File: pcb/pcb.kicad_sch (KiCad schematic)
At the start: 41 parts, among them J1 NMJ4HCD2, J2 NMJ4HCD2, J3 694106301002, SW1 FSWITCH, U1 RC4558, U2 L78L09_TO92

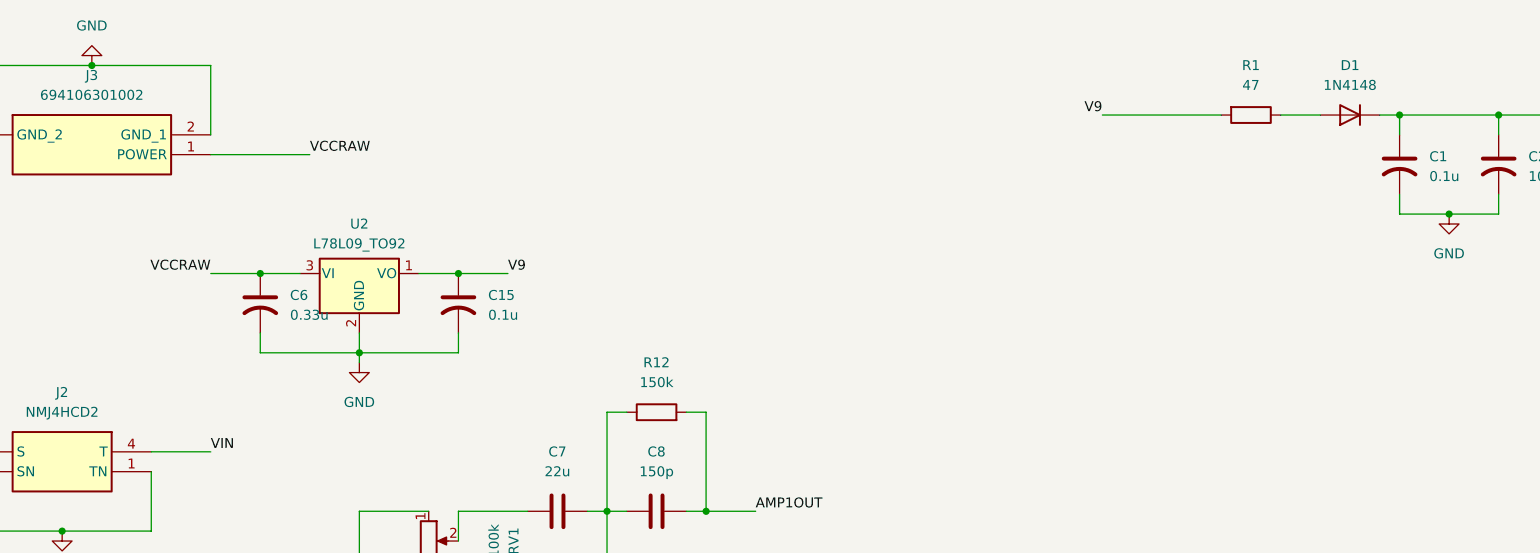
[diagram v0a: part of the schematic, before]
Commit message: Fix reverse polarity protection diode - Move ahead of regulator
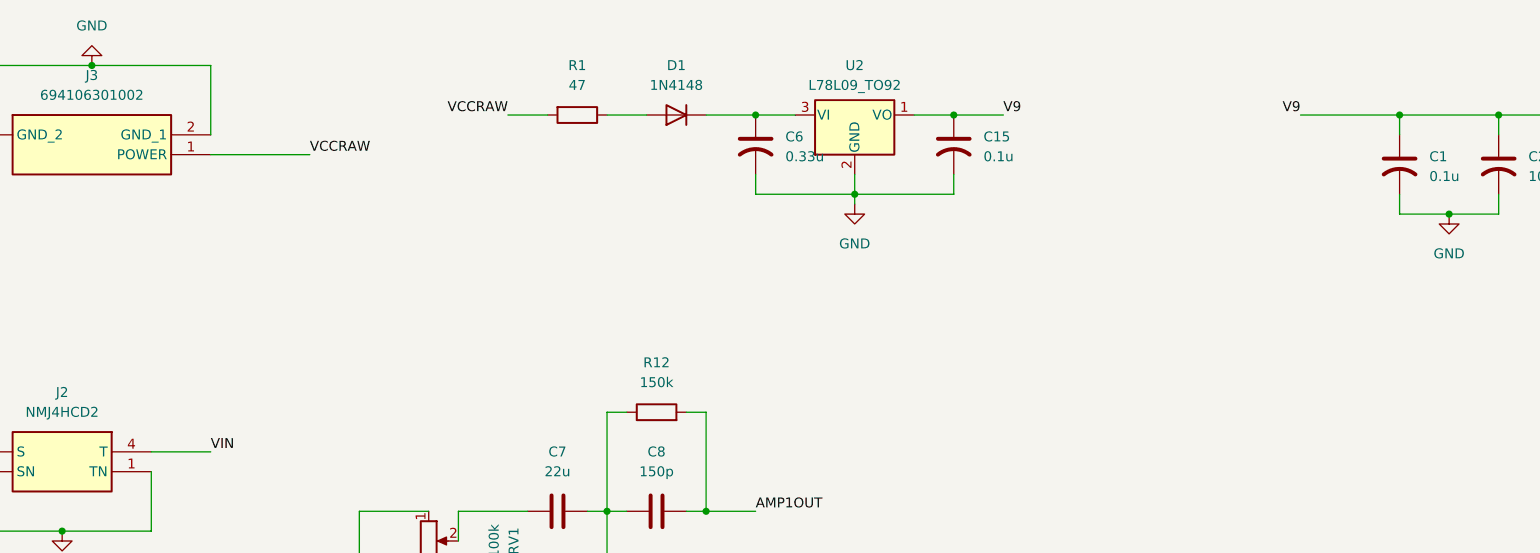
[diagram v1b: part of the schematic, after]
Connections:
- net V9: now also C1.1, C14.2, C2.1, R2.1, SW1.4, U1.8 (V+); no longer R1.2
- net VCCRAW: now also R1.2; no longer C6.1, U2.3 (VI)
- removed net VCC: C1.1, C14.2, C2.1, D1.1 (K), R2.1, SW1.4, U1.8 (V+)
- new net: C6.1, D1.1 (K), U2.3 (VI)
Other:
- moved on the sheet: C15, C6, D1, R1, U2
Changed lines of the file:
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@@
 	)
 	(junction
-		(at 203.2 25.4)
-		(diameter 0)
-		(color 0 0 0 0)
-	)
-	(junction
 		(at 101.6 76.2)
 		(diameter 0)
@@
 	)
 	(junction
-		(at 82.55 45.72)
+		(at 146.05 25.4)
 		(diameter 0)
 		(color 0 0 0 0)
@@
 	)
 	(junction
-		(at 69.85 55.88)
+		(at 203.2 25.4)
+		(diameter 0)
+		(color 0 0 0 0)
+	)
+	(junction
+		(at 133.35 35.56)
 		(diameter 0)
 		(color 0 0 0 0)
@@
 	)
 	(junction
-		(at 57.15 45.72)
+		(at 120.65 25.4)
 		(diameter 0)
 		(color 0 0 0 0)
@@
 	(wire
 		(pts
-			(xy 200.66 25.4) (xy 203.2 25.4)
-		)
-		(stroke
-			(width 0)
-			(type default)
-		)
-	)
-	(wire
-		(pts
 			(xy 99.06 76.2) (xy 101.6 76.2)
 		)
@@
 	(wire
 		(pts
-			(xy 57.15 45.72) (xy 62.23 45.72)
+			(xy 120.65 25.4) (xy 125.73 25.4)
 		)
 		(stroke
@@
 	(wire
 		(pts
-			(xy 69.85 53.34) (xy 69.85 55.88)
+			(xy 133.35 33.02) (xy 133.35 35.56)
 		)
 		(stroke
@@
 	(wire
 		(pts
-			(xy 187.96 25.4) (xy 193.04 25.4)
+			(xy 101.6 25.4) (xy 106.68 25.4)
 		)
 		(stroke
@@
 	(wire
 		(pts
-			(xy 50.8 45.72) (xy 57.15 45.72)
+			(xy 114.3 25.4) (xy 120.65 25.4)
 		)
 		(stroke
@@
 	(wire
 		(pts
+			(xy 88.9 25.4) (xy 93.98 25.4)
+		)
+		(stroke
+			(width 0)
+			(type default)
+		)
+	)
+	(wire
+		(pts
 			(xy 228.6 88.9) (xy 228.6 91.44)
 		)
@@
 	(wire
 		(pts
-			(xy 69.85 55.88) (xy 82.55 55.88)
+			(xy 133.35 35.56) (xy 146.05 35.56)
 		)
 		(stroke
@@
 	(wire
 		(pts
-			(xy 77.47 45.72) (xy 82.55 45.72)
+			(xy 140.97 25.4) (xy 146.05 25.4)
 		)
 		(stroke
@@
 	(wire
 		(pts
-			(xy 82.55 45.72) (xy 88.9 45.72)
+			(xy 146.05 25.4) (xy 152.4 25.4)
 		)
 		(stroke
@@
 	(wire
 		(pts
-			(xy 57.15 55.88) (xy 69.85 55.88)
+			(xy 120.65 35.56) (xy 133.35 35.56)
 		)
 		(stroke
@@
 	(wire
 		(pts
-			(xy 69.85 55.88) (xy 69.85 57.15)
+			(xy 133.35 35.56) (xy 133.35 36.83)
 		)
 		(stroke
@@
 	(wire
 		(pts
-			(xy 57.15 53.34) (xy 57.15 55.88)
+			(xy 120.65 33.02) (xy 120.65 35.56)
 		)
 		(stroke
@@
 	(wire
 		(pts
-			(xy 82.55 53.34) (xy 82.55 55.88)
-		)
-		(stroke
-			(width 0)
-			(type default)
-		)
-	)
-	(wire
-		(pts
-			(xy 165.1 25.4) (xy 180.34 25.4)
+			(xy 146.05 33.02) (xy 146.05 35.56)
 		)
 		(stroke
@@
 	(wire
 		(pts
+			(xy 190.5 25.4) (xy 203.2 25.4)
+		)
+		(stroke
+			(width 0)
+			(type default)
+		)
+	)
+	(wire
+		(pts
 			(xy 228.6 88.9) (xy 231.14 88.9)
 		)
@@
 	)
 	(label "V9"
-		(at 88.9 45.72 0)
+		(at 152.4 25.4 0)
 		(effects
 			(font
@@
 	)
 	(label "V9"
-		(at 165.1 25.4 180)
+		(at 190.5 25.4 180)
 		(effects
 			(font
@@
 	)
 	(label "VCCRAW"
-		(at 50.8 45.72 180)
+		(at 88.9 25.4 180)
 		(effects
 			(font
@@
 	(symbol
 		(lib_id "power:GND")
-		(at 69.85 57.15 0)
+		(at 133.35 36.83 0)
 		(unit 1)
 		(exclude_from_sim no)
@@
 		(fields_autoplaced yes)
 		(property "Reference" "#PWR03"
-			(at 69.85 63.5 0)
+			(at 133.35 43.18 0)
 			(effects
 				(font
@@
 		)
 		(property "Value" "GND"
-			(at 69.85 62.23 0)
+			(at 133.35 41.91 0)
 			(effects
 				(font
@@
 		)
 		(property "Footprint" ""
-			(at 69.85 57.15 0)
+			(at 133.35 36.83 0)
 			(effects
 				(font
@@
 		)
 		(property "Datasheet" ""
-			(at 69.85 57.15 0)
+			(at 133.35 36.83 0)
 			(effects
 				(font
@@
 		)
 		(property "Description" "Power symbol creates a global label with name \"GND\" , ground"
-			(at 69.85 57.15 0)
+			(at 133.35 36.83 0)
 			(effects
 				(font
@@
 	(symbol
 		(lib_id "Device:C_US")
-		(at 82.55 49.53 0)
+		(at 146.05 29.21 0)
 		(unit 1)
 		(exclude_from_sim no)
@@
 		(fields_autoplaced yes)
 		(property "Reference" "C15"
-			(at 86.36 48.5139 0)
+			(at 149.86 28.1939 0)
 			(effects
 				(font
@@
 		)
 		(property "Value" "0.1u"
-			(at 86.36 51.0539 0)
+			(at 149.86 30.7339 0)
 			(effects
 				(font
@@
 		)
 		(property "Footprint" "Capacitor_THT:C_Radial_D5.0mm_H11.0mm_P2.00mm"
-			(at 82.55 49.53 0)
+			(at 146.05 29.21 0)
 			(effects
 				(font
@@
 		)
 		(property "Datasheet" ""
-			(at 82.55 49.53 0)
+			(at 146.05 29.21 0)
 			(effects
 				(font
@@
 		)
 		(property "Description" "capacitor, US symbol"
-			(at 82.55 49.53 0)
+			(at 146.05 29.21 0)
 			(effects
 				(font
@@
 	(symbol
 		(lib_id "Device:R")
-		(at 184.15 25.4 270)
+		(at 97.79 25.4 270)
 		(unit 1)
 		(exclude_from_sim no)
@@
 		(fields_autoplaced yes)
 		(property "Reference" "R1"
-			(at 184.15 19.05 90)
+			(at 97.79 19.05 90)
 			(effects
 				(font
@@
 		)
 		(property "Value" "47"
-			(at 184.15 21.59 90)
+			(at 97.79 21.59 90)
 			(effects
 				(font
@@
 		)
 		(property "Footprint" "Resistor_THT:R_Axial_DIN0207_L6.3mm_D2.5mm_P10.16mm_Horizontal"
-			(at 184.15 23.622 90)
+			(at 97.79 23.622 90)
 			(effects
 				(font
@@
 		)
 		(property "Datasheet" "~"
-			(at 184.15 25.4 0)
+			(at 97.79 25.4 0)
 			(effects
 				(font
@@
 		)
 		(property "Description" "Resistor"
-			(at 184.15 25.4 0)
+			(at 97.79 25.4 0)
 			(effects
 				(font
@@
 	(symbol
 		(lib_id "Regulator_Linear:L78L09_TO92")
-		(at 69.85 45.72 0)
+		(at 133.35 25.4 0)
 		(unit 1)
 		(exclude_from_sim no)
@@
 		(fields_autoplaced yes)
 		(property "Reference" "U2"
-			(at 69.85 39.37 0)
+			(at 133.35 19.05 0)
 			(effects
 				(font
@@
 		)
 		(property "Value" "L78L09_TO92"
-			(at 69.85 41.91 0)
+			(at 133.35 21.59 0)
 			(effects
 				(font
@@
 		)
 		(property "Footprint" "Package_TO_SOT_THT:TO-92_Inline"
-			(at 69.85 40.005 0)
+			(at 133.35 19.685 0)
 			(effects
 				(font
@@
 		)
 		(property "Datasheet" "http://www.st.com/content/ccc/resource/technical/document/datasheet/15/55/e5/aa/23/5b/43/fd/CD00000446.pdf/files/CD00000446.pdf/jcr:content/translations/en.CD00000446.pdf"
-			(at 69.85 46.99 0)
+			(at 133.35 26.67 0)
 			(effects
 				(font
@@
 		)
 		(property "Description" "Positive 100mA 30V Linear Regulator, Fixed Output 9V, TO-92"
-			(at 69.85 45.72 0)
+			(at 133.35 25.4 0)
 			(effects
 				(font
@@
 	(symbol
 		(lib_id "Diode:1N4148")
-		(at 196.85 25.4 180)
+		(at 110.49 25.4 180)
 		(unit 1)
 		(exclude_from_sim no)
@@
 		(fields_autoplaced yes)
 		(property "Reference" "D1"
-			(at 196.85 19.05 0)
+			(at 110.49 19.05 0)
 			(effects
 				(font
@@
 		)
 		(property "Value" "1N4148"
-			(at 196.85 21.59 0)
+			(at 110.49 21.59 0)
 			(effects
 				(font
@@
 		)
 		(property "Footprint" "Diode_THT:D_DO-35_SOD27_P7.62mm_Horizontal"
-			(at 196.85 25.4 0)
+			(at 110.49 25.4 0)
 			(effects
 				(font
@@
 		)
 		(property "Datasheet" "https://assets.nexperia.com/documents/data-sheet/1N4148_1N4448.pdf"
-			(at 196.85 25.4 0)
+			(at 110.49 25.4 0)
 			(effects
 				(font
@@
 		)
 		(property "Description" "100V 0.15A standard switching diode, DO-35"
-			(at 196.85 25.4 0)
+			(at 110.49 25.4 0)
 			(effects
 				(font
@@
 		)
 		(property "Sim.Device" "D"
-			(at 196.85 25.4 0)
+			(at 110.49 25.4 0)
 			(effects
 				(font
@@
 		)
 		(property "Sim.Pins" "1=K 2=A"
-			(at 196.85 25.4 0)
+			(at 110.49 25.4 0)
 			(effects
 				(font
@@
 	(symbol
 		(lib_id "Device:C_US")
-		(at 57.15 49.53 0)
+		(at 120.65 29.21 0)
 		(unit 1)
 		(exclude_from_sim no)
@@
 		(fields_autoplaced yes)
 		(property "Reference" "C6"
-			(at 60.96 48.5139 0)
+			(at 124.46 28.1939 0)
 			(effects
 				(font
@@
 		)
 		(property "Value" "0.33u"
-			(at 60.96 51.0539 0)
+			(at 124.46 30.7339 0)
 			(effects
 				(font
@@
 		)
 		(property "Footprint" "Capacitor_THT:C_Radial_D5.0mm_H11.0mm_P2.00mm"
-			(at 57.15 49.53 0)
+			(at 120.65 29.21 0)
 			(effects
 				(font
@@
 		)
 		(property "Datasheet" ""
-			(at 57.15 49.53 0)
+			(at 120.65 29.21 0)
 			(effects
 				(font
@@
 		)
 		(property "Description" "capacitor, US symbol"
-			(at 57.15 49.53 0)
+			(at 120.65 29.21 0)
 			(effects
 				(font
